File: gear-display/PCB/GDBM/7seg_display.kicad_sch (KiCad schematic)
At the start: 13 parts

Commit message: new features
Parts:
- removed Q?: PMOS_30V_250mA_RSC002P03T316, KD_Package_TO_SOT_SMD:SOT95P230X100-3N, symbol KD_Transistor_FET:PMOS_30V_250mA_RSC002P03T316
- added Q?: PMOS_30V_4A1_SIL3407-TP, KD_Package_TO_SOT_SMD:SOT95P280X120-6RN, symbol KD_Transistor_FET:PMOS_30V_4A1_SIL3407-TP
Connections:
- net +12V: now also Q?.1 (D), Q?.2 (D), Q?.5 (D), Q?.6 (D)
- net 12V_PWM: now reaches D?.1 (K), D?.5 (C)
- net 12V_PWM: now also Q?.4 (S)
- net at U?.5 (OUT): now also Q?.3 (G)
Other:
- moved on the sheet: C?, D?, R?, U?

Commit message: updates
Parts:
- removed R? (x8): R_0805_1200_5%, KD_Resistor:R_0805_2012Metric, symbol KD_Resistor:R_0805_1200_5%
- added R? (x8): R_1206_191_1%, KD_Resistor:RESC3216X70N, symbol KD_Resistor:R_1206_191_1%
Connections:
- net a: now also R?.1
- net b: now also R?.1
- net c: now also R?.1
- net d: now also R?.1
- net dp: now also R?.1
- net e: now also R?.1
- net f: now also R?.1
- net g: now also R?.1
- net at D?.7 (Aa): now also R?.2
- net at D?.2 (Ae): now also R?.2
- net at D?.10 (Ag): now also R?.2
- net at D?.3 (Ad): now also R?.2
- net at D?.4 (Ac): now also R?.2
- net at D?.6 (Ab): now also R?.2
- net at D?.8 (Adp): now also R?.2
- net at D?.9 (Af): now also R?.2

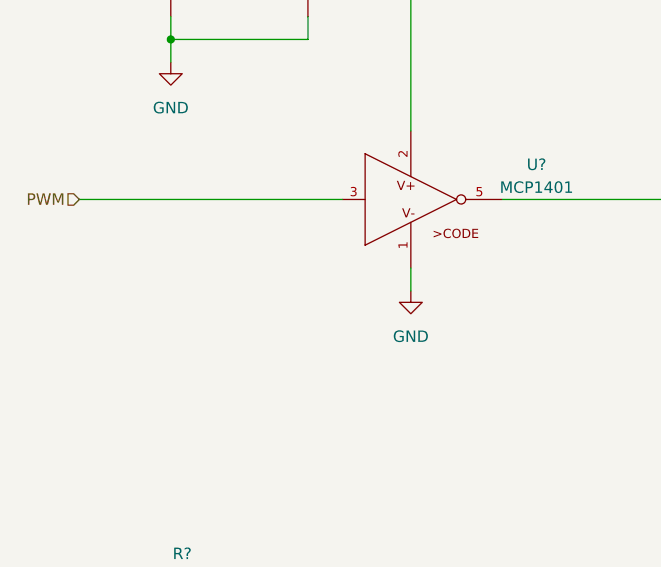
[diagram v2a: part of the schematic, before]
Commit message: changed to match simhub conf
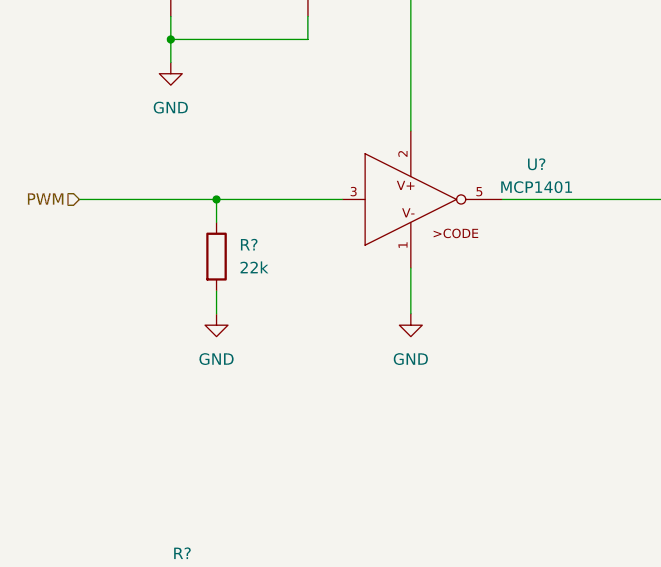
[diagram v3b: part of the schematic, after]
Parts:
- added R?: R_0603_22k_1%, KD_Resistor:R_0603_1608Metric, symbol KD_Resistor:R_0603_22k_1%
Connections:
- net GND: now also R?.2
- net PWM: now also R?.1
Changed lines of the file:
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@@
   (junction (at 173.99 72.39) (diameter 0) (color 0 0 0 0)
   )
+  (junction (at 106.68 59.69) (diameter 0) (color 0 0 0 0)
+  )
   (junction (at 101.6 41.91) (diameter 0) (color 0 0 0 0)
   )
@@
     (stroke (width 0) (type default) (color 0 0 0 0))
   )
+  (wire (pts (xy 106.68 59.69) (xy 106.68 62.23))
+    (stroke (width 0) (type default) (color 0 0 0 0))
+  )
   (wire (pts (xy 153.67 154.94) (xy 203.2 154.94))
     (stroke (width 0) (type default) (color 0 0 0 0))
@@
     (stroke (width 0) (type default) (color 0 0 0 0))
   )
-  (wire (pts (xy 128.27 67.31) (xy 128.27 69.85))
+  (wire (pts (xy 128.27 67.31) (xy 128.27 72.39))
     (stroke (width 0) (type default) (color 0 0 0 0))
   )
@@
     (stroke (width 0) (type default) (color 0 0 0 0))
   )
+  (wire (pts (xy 106.68 69.85) (xy 106.68 72.39))
+    (stroke (width 0) (type default) (color 0 0 0 0))
+  )
   (wire (pts (xy 115.57 167.64) (xy 228.6 167.64))
     (stroke (width 0) (type default) (color 0 0 0 0))
@@
     (stroke (width 0) (type default) (color 0 0 0 0))
   )
+  (wire (pts (xy 106.68 59.69) (xy 120.65 59.69))
+    (stroke (width 0) (type default) (color 0 0 0 0))
+  )
   (wire (pts (xy 153.67 123.19) (xy 153.67 154.94))
     (stroke (width 0) (type default) (color 0 0 0 0))
@@
     (stroke (width 0) (type default) (color 0 0 0 0))
   )
-  (wire (pts (xy 91.44 59.69) (xy 120.65 59.69))
+  (wire (pts (xy 91.44 59.69) (xy 106.68 59.69))
     (stroke (width 0) (type default) (color 0 0 0 0))
   )
@@
     (pin "2")
   )
+  (symbol (lib_id "KD_Resistor:R_0603_22k_1%") (at 106.68 66.04 0) (unit 1)
+    (in_bom yes) (on_board yes)
+    (property "Reference" "R?" (id 0) (at 109.22 64.77 0)
+      (effects (font (size 1.27 1.27)) (justify left))
+    )
+    (property "Value" "R_0603_22k_1%" (id 1) (at 93.98 34.29 0)
+      (effects (font (size 1.27 1.27)) (justify left) hide)
+    )
+    (property "Footprint" "KD_Resistor:R_0603_1608Metric" (id 2) (at 93.98 52.07 0)
+      (effects (font (size 1.27 1.27)) (justify left) hide)
+    )
+    (property "Datasheet" "https://www.yageo.com/upload/media/product/productsearch/datasheet/rchip/PYu-RC_Group_51_RoHS_L_11.pdf" (id 3) (at 93.98 54.61 0)
+      (effects (font (size 1.27 1.27)) (justify left) hide)
+    )
+    (property "Code" "22k" (id 4) (at 109.22 67.31 0)
+      (effects (font (size 1.27 1.27)) (justify left))
+    )
+    (property "Manufacturer" "YAGEO" (id 5) (at 93.98 36.83 0)
+      (effects (font (size 1.27 1.27)) (justify left) hide)
+    )
+    (property "MFG_PartNo" "311-22.0KHRCT-ND" (id 6) (at 93.98 39.37 0)
+      (effects (font (size 1.27 1.27)) (justify left) hide)
+    )
+    (property "Supplier" "Digi-Key" (id 7) (at 93.98 41.91 0)
+      (effects (font (size 1.27 1.27)) (justify left) hide)
+    )
+    (property "Supplier_PartNo" "311-22.0KHRCT-ND" (id 8) (at 93.98 44.45 0)
+      (effects (font (size 1.27 1.27)) (justify left) hide)
+    )
+    (property "DNP" "F" (id 9) (at 93.98 46.99 0)
+      (effects (font (size 1.27 1.27)) (justify left) hide)
+    )
+    (property "Price" "0.01" (id 10) (at 93.98 49.53 0)
+      (effects (font (size 1.27 1.27)) (justify left) hide)
+    )
+    (pin "1")
+    (pin "2")
+  )
   (symbol (lib_id "KD_Resistor:R_1206_191_1%") (at 102.87 105.41 90) (unit 1)
     (in_bom yes) (on_board yes) (fields_autoplaced)
@@
     (pin "2")
   )
-  (symbol (lib_id "power:GND") (at 128.27 69.85 0) (unit 1)
-    (in_bom yes) (on_board yes) (fields_autoplaced)
-    (property "Reference" "#PWR?" (id 0) (at 128.27 76.2 0)
-      (effects (font (size 1.27 1.27)) hide)
-    )
-    (property "Value" "GND" (id 1) (at 128.27 74.93 0))
-    (property "Footprint" "" (id 2) (at 128.27 69.85 0)
-      (effects (font (size 1.27 1.27)) hide)
-    )
-    (property "Datasheet" "" (id 3) (at 128.27 69.85 0)
+  (symbol (lib_id "power:GND") (at 128.27 72.39 0) (unit 1)
+    (in_bom yes) (on_board yes) (fields_autoplaced)
+    (property "Reference" "#PWR?" (id 0) (at 128.27 78.74 0)
+      (effects (font (size 1.27 1.27)) hide)
+    )
+    (property "Value" "GND" (id 1) (at 128.27 77.47 0))
+    (property "Footprint" "" (id 2) (at 128.27 72.39 0)
+      (effects (font (size 1.27 1.27)) hide)
+    )
+    (property "Datasheet" "" (id 3) (at 128.27 72.39 0)
       (effects (font (size 1.27 1.27)) hide)
     )
@@
     (pin "6")
   )
+  (symbol (lib_id "power:GND") (at 106.68 72.39 0) (unit 1)
+    (in_bom yes) (on_board yes) (fields_autoplaced)
+    (property "Reference" "#PWR?" (id 0) (at 106.68 78.74 0)
+      (effects (font (size 1.27 1.27)) hide)
+    )
+    (property "Value" "GND" (id 1) (at 106.68 77.47 0))
+    (property "Footprint" "" (id 2) (at 106.68 72.39 0)
+      (effects (font (size 1.27 1.27)) hide)
+    )
+    (property "Datasheet" "" (id 3) (at 106.68 72.39 0)
+      (effects (font (size 1.27 1.27)) hide)
+    )
+    (pin "1")
+  )
   (symbol (lib_id "KD_Resistor:R_1206_191_1%") (at 102.87 140.97 90) (unit 1)

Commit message: rikki
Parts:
- removed R?: R_0603_22k_1%, KD_Resistor:R_0603_1608Metric, symbol KD_Resistor:R_0603_22k_1%
- added R15: R_0603_22k_1%, KD_Resistor:RESC1608X55N, symbol KD_Resistor:R_0603_22k_1%
- added R30: R_0603_DNP, KD_Resistor:RESC1608X55N_DNP, symbol KD_Resistor:R_0603_DNP
- C14: renamed from C?; value C_0603_100n_X7R_50V -> C_0603_100n_X7R_100V; symbol KD_Capacitor:C_0603_100n_X7R_50V -> KD_Capacitor:C_0603_100n_X7R_100V; MFG_PartNo CL10B104KB8NNWC -> CL10B104KC8NNNC; Manufacturer Samsung -> Samsung Electro-Mechanics; Price 0.01 -> 0.03; Supplier_PartNo 1276-1935-1-ND -> 1276-6807-1-ND
- C15: renamed from C?; value C_0805_1u_X7R_25V -> C_0805_DNP
- U3: renamed from U?; footprint KD_Package_TO_SOT_SMD:SOT95P280X145-5N_SOT23-5 -> KD_Package_TO_SOT_SMD:SOT95P280X145-5N
- gave numbers to parts that had none: 10
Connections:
- net GND: now also R30.2
- net PWM: now also R15.2, R30.1
- new net +5V: R15.1

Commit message: PSU and LED powering changed
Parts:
- C14: footprint KD_Capacitor:C_0603_1608Metric -> KD_Capacitor:CAPC1608X90N
- C15: footprint KD_Capacitor:C_0805_2012Metric_DNP -> KD_Capacitor:CAPC2012X135N_DNP
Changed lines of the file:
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@@
       (effects (font (size 1.27 1.27)) (justify left) hide)
     )
-    (property "Footprint" "KD_Capacitor:C_0603_1608Metric" (id 2) (at 88.9 21.59 0)
+    (property "Footprint" "KD_Capacitor:CAPC1608X90N" (id 2) (at 88.9 21.59 0)
       (effects (font (size 1.27 1.27)) (justify left) hide)
     )
@@
       (effects (font (size 1.27 1.27)) (justify left) hide)
     )
-    (property "Footprint" "KD_Capacitor:C_0805_2012Metric_DNP" (id 2) (at 104.14 21.59 0)
+    (property "Footprint" "KD_Capacitor:CAPC2012X135N_DNP" (id 2) (at 104.14 21.59 0)
       (effects (font (size 1.27 1.27)) (justify left) hide)
     )

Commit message: R33 value change
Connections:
- net +12V: now also Q1.4 (S); no longer Q1.1 (D), Q1.2 (D), Q1.5 (D), Q1.6 (D)
- net 12V_PWM: now also Q1.1 (D), Q1.2 (D), Q1.5 (D), Q1.6 (D); no longer Q1.4 (S)
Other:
- note added: "Pitäiskö vaihtaa MCP1402, jotta säätö olis 0-50 %"
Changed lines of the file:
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@@
     (stroke (width 0) (type default))
+  )
+  (text "Pitäiskö vaihtaa MCP1402, jotta säätö olis 0-50 %" (at 95.25 83.82 0)
+    (effects (font (size 2 2)) (justify left bottom))
   )
   (hierarchical_label "PWM" (shape input) (at 73.66 59.69 180) (fields_autoplaced)
@@
         (path "/e63e39d7-6ac0-4ffd-8aa3-1841a4541b55/67e35e0a-77e9-4a25-928b-43c27de68dee"
           (reference "R15") (unit 1)
+        )
+      )
+    )
+  )
+  (symbol (lib_id "KD_Transistor_FET:PMOS_30V_4A1_SIL3407-TP") (at 171.45 59.69 0) (mirror x) (unit 1)
+    (in_bom yes) (on_board yes) (dnp no)
+    (property "Reference" "Q1" (at 177.8 60.9601 0)
+      (effects (font (size 1.27 1.27)) (justify left))
+    )
+    (property "Value" "PMOS_30V_4A1_SIL3407-TP" (at 158.75 96.52 0)
+      (effects (font (size 1.27 1.27)) (justify left) hide)
+    )
+    (property "Footprint" "KD_Package_TO_SOT_SMD:SOT95P280X120-6RN" (at 158.75 78.74 0)
+      (effects (font (size 1.27 1.27)) (justify left) hide)
+    )
+    (property "Datasheet" "https://www.mccsemi.com/pdf/Products/SIL3407(SOT23-6L).pdf" (at 158.75 76.2 0)
+      (effects (font (size 1.27 1.27)) (justify left) hide)
+    )
+    (property "Code" "SIL3407-TP" (at 177.8 58.4201 0)
+      (effects (font (size 1.27 1.27)) (justify left))
+    )
+    (property "Manufacturer" "Micro Commercial Co" (at 158.75 93.98 0)
+      (effects (font (size 1.27 1.27)) (justify left) hide)
+    )
+    (property "MFG_PartNo" "SIL3407-TP" (at 158.75 91.44 0)
+      (effects (font (size 1.27 1.27)) (justify left) hide)
+    )
+    (property "Supplier" "Digi-Key" (at 158.75 88.9 0)
+      (effects (font (size 1.27 1.27)) (justify left) hide)
+    )
+    (property "Supplier_PartNo" "353-SIL3407-TPCT-ND" (at 158.75 86.36 0)
+      (effects (font (size 1.27 1.27)) (justify left) hide)
+    )
+    (property "DNP" "F" (at 158.75 83.82 0)
+      (effects (font (size 1.27 1.27)) (justify left) hide)
+    )
+    (property "Price" "0.4" (at 158.75 81.28 0)
+      (effects (font (size 1.27 1.27)) (justify left) hide)
+    )
+    (pin "1")
+    (pin "2")
+    (pin "3")
+    (pin "4")
+    (pin "5")
+    (pin "6")
+    (instances
+      (project "GDBM"
+        (path "/e63e39d7-6ac0-4ffd-8aa3-1841a4541b55/67e35e0a-77e9-4a25-928b-43c27de68dee"
+          (reference "Q1") (unit 1)
         )
       )
@@
         )
       )
-    )
-  )
-  (symbol (lib_id "KD_Transistor_FET:PMOS_30V_4A1_SIL3407-TP") (at 171.45 59.69 0) (unit 1)
-    (in_bom yes) (on_board yes) (dnp no) (fields_autoplaced)
-    (property "Reference" "Q1" (at 177.8 58.4199 0)
-      (effects (font (size 1.27 1.27)) (justify left))
-    )
-    (property "Value" "PMOS_30V_4A1_SIL3407-TP" (at 158.75 22.86 0)
-      (effects (font (size 1.27 1.27)) (justify left) hide)
-    )
-    (property "Footprint" "KD_Package_TO_SOT_SMD:SOT95P280X120-6RN" (at 158.75 40.64 0)
-      (effects (font (size 1.27 1.27)) (justify left) hide)
-    )
-    (property "Datasheet" "https://www.mccsemi.com/pdf/Products/SIL3407(SOT23-6L).pdf" (at 158.75 43.18 0)
-      (effects (font (size 1.27 1.27)) (justify left) hide)
-    )
-    (property "Code" "SIL3407-TP" (at 177.8 60.9599 0)
-      (effects (font (size 1.27 1.27)) (justify left))
-    )
-    (property "Manufacturer" "Micro Commercial Co" (at 158.75 25.4 0)
-      (effects (font (size 1.27 1.27)) (justify left) hide)
-    )
-    (property "MFG_PartNo" "SIL3407-TP" (at 158.75 27.94 0)
-      (effects (font (size 1.27 1.27)) (justify left) hide)
-    )
-    (property "Supplier" "Digi-Key" (at 158.75 30.48 0)
-      (effects (font (size 1.27 1.27)) (justify left) hide)
-    )
-    (property "Supplier_PartNo" "353-SIL3407-TPCT-ND" (at 158.75 33.02 0)
-      (effects (font (size 1.27 1.27)) (justify left) hide)
-    )
-    (property "DNP" "F" (at 158.75 35.56 0)
-      (effects (font (size 1.27 1.27)) (justify left) hide)
-    )
-    (property "Price" "0.4" (at 158.75 38.1 0)
-      (effects (font (size 1.27 1.27)) (justify left) hide)
-    )
-    (pin "1")
-    (pin "2")
-    (pin "3")
-    (pin "4")
-    (pin "5")
-    (pin "6")
-    (instances
-      (project "GDBM"
-        (path "/e63e39d7-6ac0-4ffd-8aa3-1841a4541b55/67e35e0a-77e9-4a25-928b-43c27de68dee"
-          (reference "Q1") (unit 1)
-        )
-      )
